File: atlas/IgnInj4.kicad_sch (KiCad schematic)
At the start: 7 parts, among them U1401 MC33810

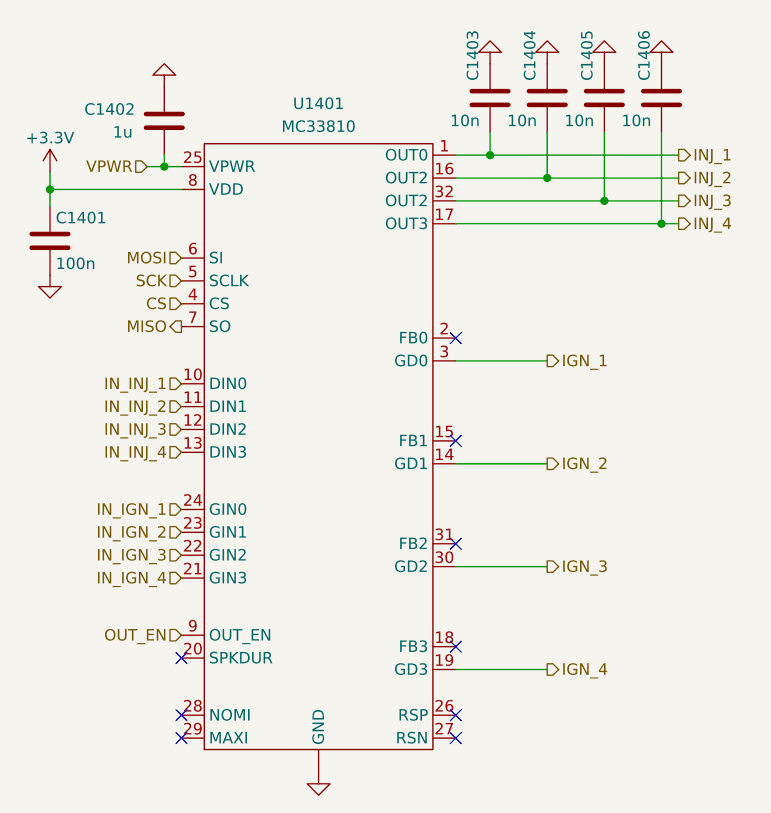
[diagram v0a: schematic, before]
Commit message: footprints & lcsc
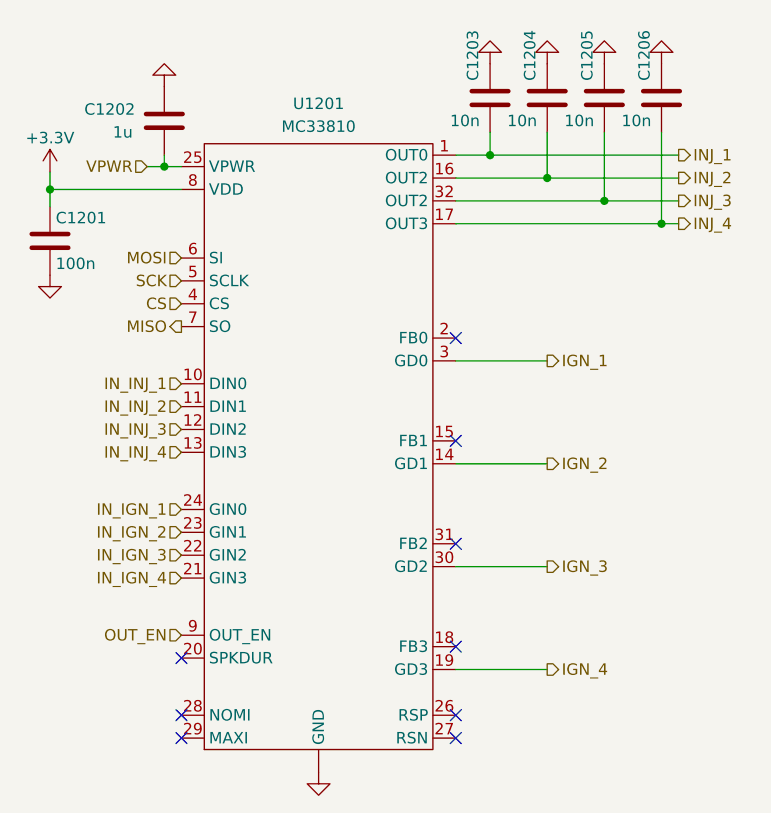
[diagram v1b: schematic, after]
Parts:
- C1201: renamed from C1401; footprint Capacitor_SMD:C_0402_1005Metric -> Capacitor_SMD:C_0603_1608Metric; LCSC (none) -> C14663
- renumbered C1402 to C1202, C1403 to C1203, C1404 to C1204, C1405 to C1205, C1406 to C1206, U1401 to U1201
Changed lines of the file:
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@@
   (symbol (lib_id "Device:C") (at 32.385 46.99 0)
     (in_bom yes) (on_board yes)
-    (property "Reference" "C1401" (id 0) (at 33.02 44.4499 0)
+    (property "Reference" "C1201" (id 0) (at 33.02 44.4499 0)
       (effects (font (size 1.27 1.27)) (justify left))
     )
@@
       (effects (font (size 1.27 1.27)) (justify left))
     )
-    (property "Footprint" "Capacitor_SMD:C_0402_1005Metric" (id 2) (at 33.3502 50.8 0)
+    (property "Footprint" "Capacitor_SMD:C_0603_1608Metric" (id 2) (at 33.3502 50.8 0)
       (effects (font (size 1.27 1.27)) hide)
     )
     (property "Datasheet" "~" (id 3) (at 32.385 46.99 0)
+      (effects (font (size 1.27 1.27)) hide)
+    )
+    (property "LCSC" "C14663" (id 4) (at 32.385 46.99 0)
       (effects (font (size 1.27 1.27)) hide)
     )
@@
   (symbol (lib_id "Device:C") (at 45.085 33.655 180)
     (in_bom yes) (on_board yes)
-    (property "Reference" "C1402" (id 0) (at 36.195 32.3849 0)
+    (property "Reference" "C1202" (id 0) (at 36.195 32.3849 0)
       (effects (font (size 1.27 1.27)) (justify right))
     )
@@
   (symbol (lib_id "Device:C") (at 81.28 31.115 0)
     (in_bom yes) (on_board yes)
-    (property "Reference" "C1403" (id 0) (at 79.375 29.2099 90)
+    (property "Reference" "C1203" (id 0) (at 79.375 29.2099 90)
       (effects (font (size 1.27 1.27)) (justify left))
     )
@@
   (symbol (lib_id "Device:C") (at 87.63 31.115 0)
     (in_bom yes) (on_board yes)
-    (property "Reference" "C1404" (id 0) (at 85.725 29.2099 90)
+    (property "Reference" "C1204" (id 0) (at 85.725 29.2099 90)
       (effects (font (size 1.27 1.27)) (justify left))
     )
@@
   (symbol (lib_id "Device:C") (at 93.98 31.115 0)
     (in_bom yes) (on_board yes)
-    (property "Reference" "C1405" (id 0) (at 92.075 29.2099 90)
+    (property "Reference" "C1205" (id 0) (at 92.075 29.2099 90)
       (effects (font (size 1.27 1.27)) (justify left))
     )
@@
   (symbol (lib_id "Device:C") (at 100.33 31.115 0)
     (in_bom yes) (on_board yes)
-    (property "Reference" "C1406" (id 0) (at 98.425 29.2099 90)
+    (property "Reference" "C1206" (id 0) (at 98.425 29.2099 90)
       (effects (font (size 1.27 1.27)) (justify left))
     )
@@
   (symbol (lib_id "mc33810:MC33810") (at 58.42 46.355 0)
     (in_bom yes) (on_board yes) (fields_autoplaced)
-    (property "Reference" "U1401" (id 0) (at 62.23 31.75 0))
+    (property "Reference" "U1201" (id 0) (at 62.23 31.75 0))
     (property "Value" "MC33810" (id 1) (at 62.23 34.29 0))
     (property "Footprint" "Package_SO:SOIC-8-1EP_3.9x4.9mm_P1.27mm_EP2.29x3mm" (id 2) (at 58.42 46.355 0)
